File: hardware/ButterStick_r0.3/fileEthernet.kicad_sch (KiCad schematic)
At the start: 56 parts, among them CON1 JD1_0001NL, CON2 JD1_0001NL, Q7 PMBT3904MB, Q8 PMBT3904MB, U11 KSZ9031, Y1 25Mhz

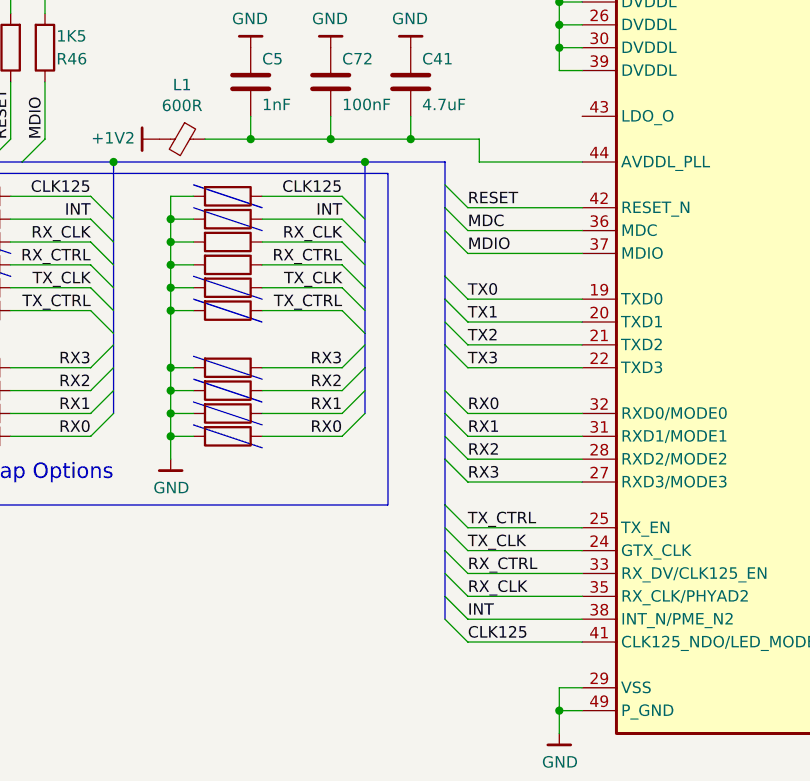
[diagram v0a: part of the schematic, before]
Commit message: hw.r0_3: routing improvements
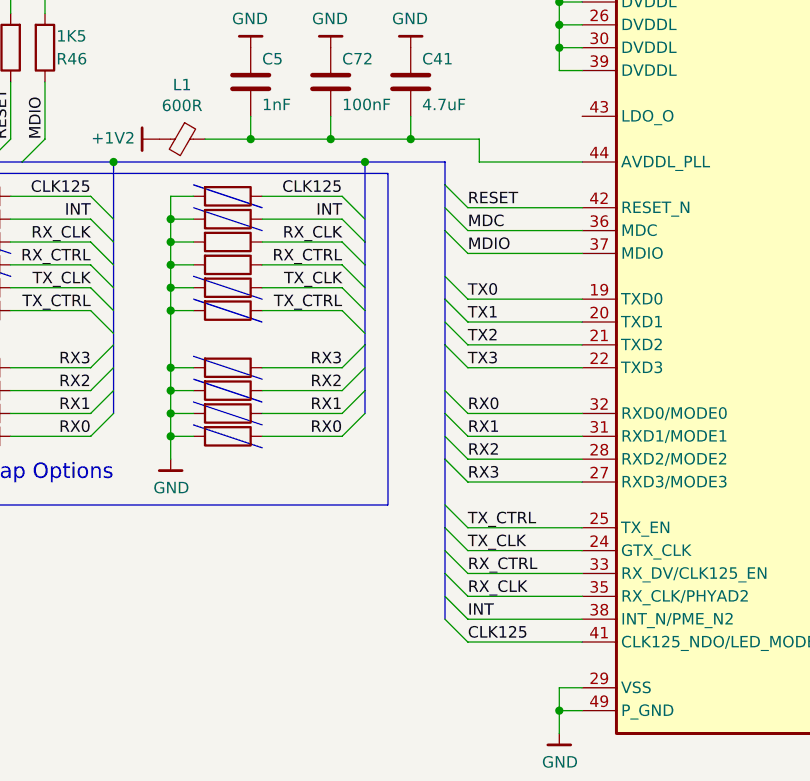
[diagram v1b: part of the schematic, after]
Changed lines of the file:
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@@
   (bus (pts (xy 111.76 91.44) (xy 111.76 100.33)))
   (bus (pts (xy 111.76 91.44) (xy 120.65 91.44)))
-  (bus (pts (xy 111.76 100.33) (xy 111.76 105.41)))
-  (bus (pts (xy 111.76 105.41) (xy 111.76 110.49)))
-  (bus (pts (xy 111.76 110.49) (xy 111.76 114.3)))
-  (bus (pts (xy 111.76 114.3) (xy 111.76 119.38)))
-  (bus (pts (xy 120.65 91.44) (xy 120.65 96.52)))
-  (bus (pts (xy 120.65 96.52) (xy 120.65 104.14)))
-  (bus (pts (xy 120.65 104.14) (xy 120.65 106.68)))
+  (bus (pts (xy 111.76 100.33) (xy 111.76 102.87)))
+  (bus (pts (xy 111.76 102.87) (xy 111.76 107.95)))
+  (bus (pts (xy 111.76 107.95) (xy 111.76 111.76)))
+  (bus (pts (xy 111.76 111.76) (xy 111.76 116.84)))
+  (bus (pts (xy 111.76 116.84) (xy 111.76 119.38)))
+  (bus (pts (xy 120.65 91.44) (xy 120.65 93.98)))
+  (bus (pts (xy 120.65 93.98) (xy 120.65 99.06)))
+  (bus (pts (xy 120.65 99.06) (xy 120.65 106.68)))
   (bus (pts (xy 120.65 106.68) (xy 120.65 111.76)))
   (bus (pts (xy 120.65 111.76) (xy 120.65 119.38)))
   (bus (pts (xy 120.65 119.38) (xy 120.65 124.46)))
-  (bus (pts (xy 120.65 124.46) (xy 120.65 129.54)))
-  (bus (pts (xy 120.65 129.54) (xy 120.65 134.62)))
-  (bus (pts (xy 120.65 134.62) (xy 120.65 139.7)))
-  (bus (pts (xy 120.65 139.7) (xy 120.65 142.24)))
+  (bus (pts (xy 120.65 124.46) (xy 120.65 132.08)))
+  (bus (pts (xy 120.65 132.08) (xy 120.65 137.16)))
+  (bus (pts (xy 120.65 137.16) (xy 120.65 142.24)))
   (polyline (pts (xy 59.69 92.71) (xy 59.69 129.54)))
   (polyline (pts (xy 59.69 92.71) (xy 114.3 92.71)))

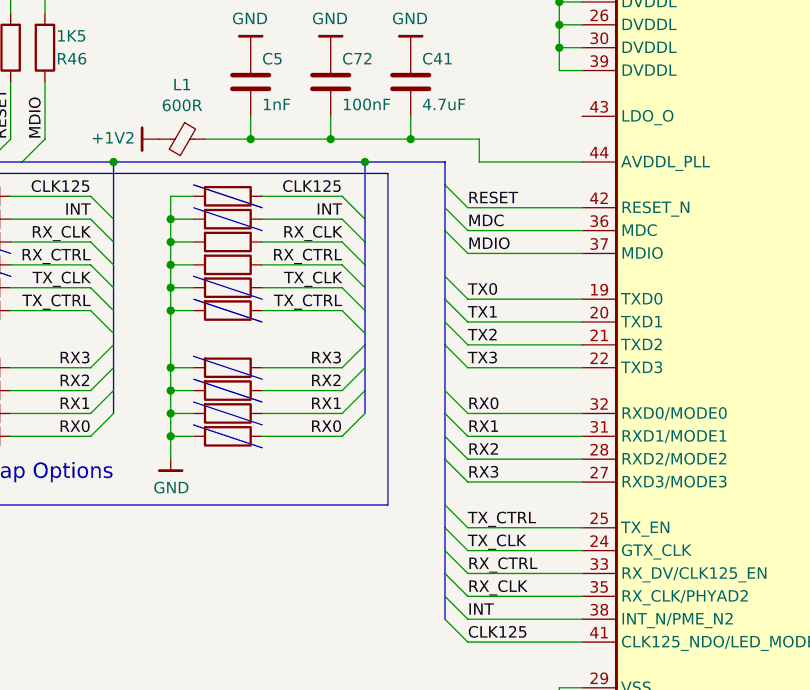
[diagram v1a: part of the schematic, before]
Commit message: hw.r0_3: Start routing DDR3 interface
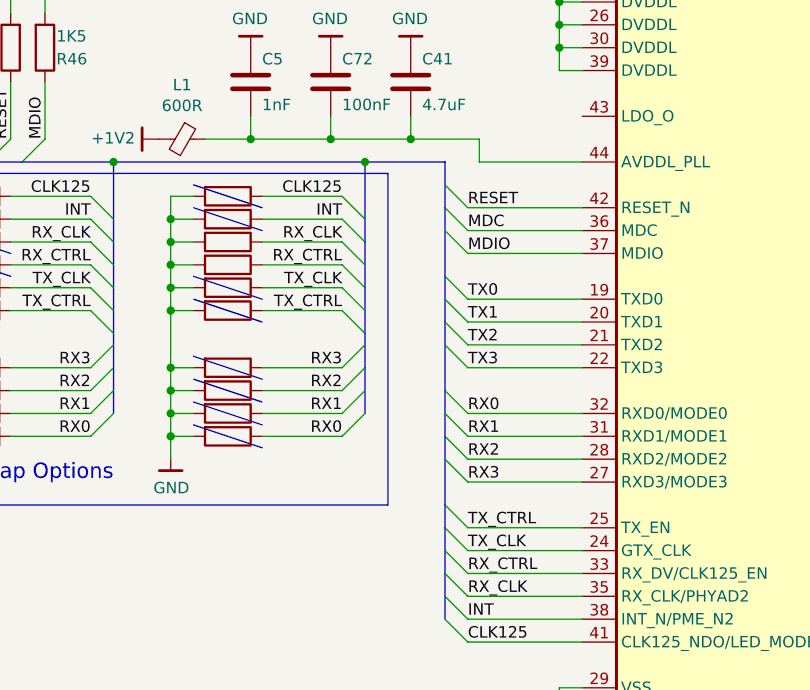
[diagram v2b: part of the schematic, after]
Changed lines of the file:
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@@
-(kicad_sch (version 20200512) (host eeschema "5.99.0-unknown-c8476d6~101~ubuntu18.04.1")
-  (page 3 20)
+(kicad_sch (version 20200512) (host eeschema "5.99.0-unknown-711fc99~101~ubuntu18.04.1")
+  (page 1 20)
   (paper "A4")
   (title_block
@@
   (bus (pts (xy 111.76 91.44) (xy 111.76 100.33)))
   (bus (pts (xy 111.76 91.44) (xy 120.65 91.44)))
-  (bus (pts (xy 111.76 100.33) (xy 111.76 102.87)))
-  (bus (pts (xy 111.76 102.87) (xy 111.76 107.95)))
-  (bus (pts (xy 111.76 107.95) (xy 111.76 111.76)))
-  (bus (pts (xy 111.76 111.76) (xy 111.76 116.84)))
-  (bus (pts (xy 111.76 116.84) (xy 111.76 119.38)))
-  (bus (pts (xy 120.65 91.44) (xy 120.65 93.98)))
-  (bus (pts (xy 120.65 93.98) (xy 120.65 99.06)))
-  (bus (pts (xy 120.65 99.06) (xy 120.65 106.68)))
-  (bus (pts (xy 120.65 106.68) (xy 120.65 111.76)))
-  (bus (pts (xy 120.65 111.76) (xy 120.65 119.38)))
-  (bus (pts (xy 120.65 119.38) (xy 120.65 124.46)))
-  (bus (pts (xy 120.65 124.46) (xy 120.65 132.08)))
+  (bus (pts (xy 111.76 100.33) (xy 111.76 105.41)))
+  (bus (pts (xy 111.76 105.41) (xy 111.76 110.49)))
+  (bus (pts (xy 111.76 110.49) (xy 111.76 114.3)))
+  (bus (pts (xy 111.76 114.3) (xy 111.76 119.38)))
+  (bus (pts (xy 120.65 91.44) (xy 120.65 96.52)))
+  (bus (pts (xy 120.65 96.52) (xy 120.65 104.14)))
+  (bus (pts (xy 120.65 104.14) (xy 120.65 109.22)))
+  (bus (pts (xy 120.65 109.22) (xy 120.65 116.84)))
+  (bus (pts (xy 120.65 116.84) (xy 120.65 121.92)))
+  (bus (pts (xy 120.65 121.92) (xy 120.65 129.54)))
+  (bus (pts (xy 120.65 129.54) (xy 120.65 132.08)))
   (bus (pts (xy 120.65 132.08) (xy 120.65 137.16)))
   (bus (pts (xy 120.65 137.16) (xy 120.65 142.24)))

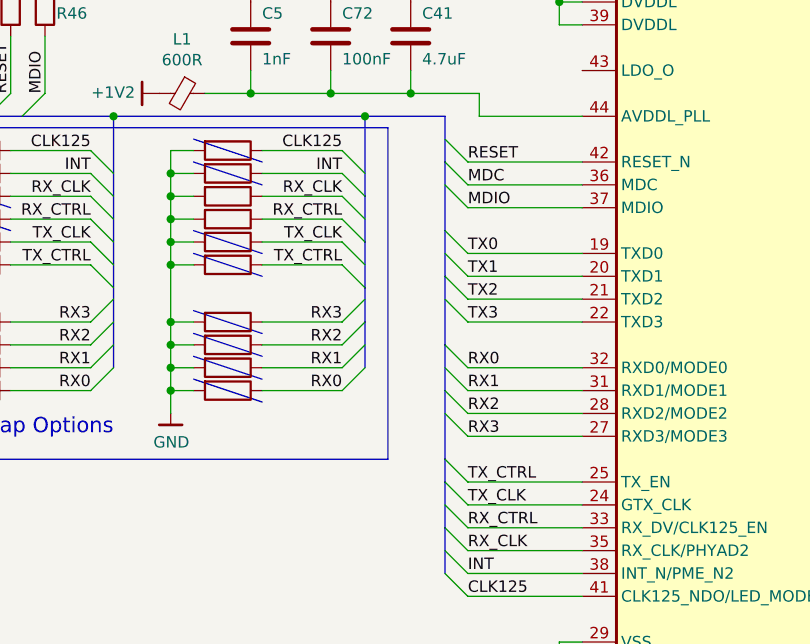
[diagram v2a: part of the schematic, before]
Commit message: hw.r0_3: Inital routing of DDR3 done
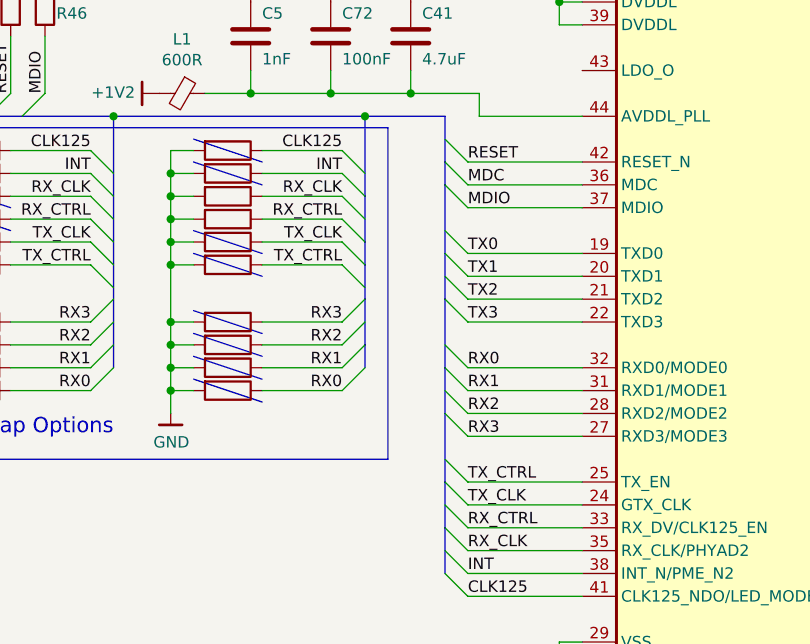
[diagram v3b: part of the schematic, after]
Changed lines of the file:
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@@
   (bus (pts (xy 111.76 91.44) (xy 120.65 91.44)))
   (bus (pts (xy 111.76 100.33) (xy 111.76 105.41)))
-  (bus (pts (xy 111.76 105.41) (xy 111.76 110.49)))
-  (bus (pts (xy 111.76 110.49) (xy 111.76 114.3)))
-  (bus (pts (xy 111.76 114.3) (xy 111.76 119.38)))
+  (bus (pts (xy 111.76 105.41) (xy 111.76 107.95)))
+  (bus (pts (xy 111.76 107.95) (xy 111.76 111.76)))
+  (bus (pts (xy 111.76 111.76) (xy 111.76 116.84)))
+  (bus (pts (xy 111.76 116.84) (xy 111.76 119.38)))
   (bus (pts (xy 120.65 91.44) (xy 120.65 96.52)))
-  (bus (pts (xy 120.65 96.52) (xy 120.65 104.14)))
-  (bus (pts (xy 120.65 104.14) (xy 120.65 109.22)))
-  (bus (pts (xy 120.65 109.22) (xy 120.65 116.84)))
-  (bus (pts (xy 120.65 116.84) (xy 120.65 121.92)))
-  (bus (pts (xy 120.65 121.92) (xy 120.65 129.54)))
-  (bus (pts (xy 120.65 129.54) (xy 120.65 132.08)))
+  (bus (pts (xy 120.65 96.52) (xy 120.65 99.06)))
+  (bus (pts (xy 120.65 99.06) (xy 120.65 106.68)))
+  (bus (pts (xy 120.65 106.68) (xy 120.65 111.76)))
+  (bus (pts (xy 120.65 111.76) (xy 120.65 119.38)))
+  (bus (pts (xy 120.65 119.38) (xy 120.65 124.46)))
+  (bus (pts (xy 120.65 124.46) (xy 120.65 132.08)))
   (bus (pts (xy 120.65 132.08) (xy 120.65 137.16)))
   (bus (pts (xy 120.65 137.16) (xy 120.65 142.24)))

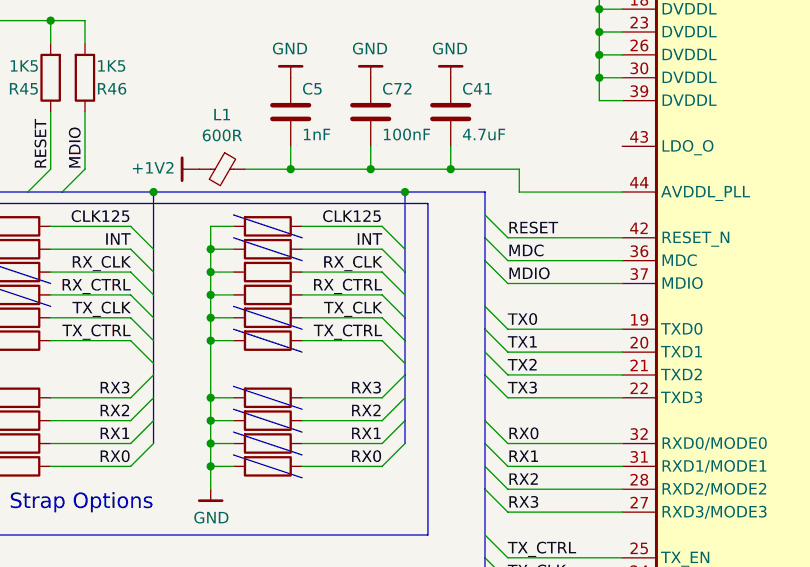
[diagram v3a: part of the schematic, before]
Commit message: hw.r0_3: routed SYZYGY, begin routing RGMII/ULPI
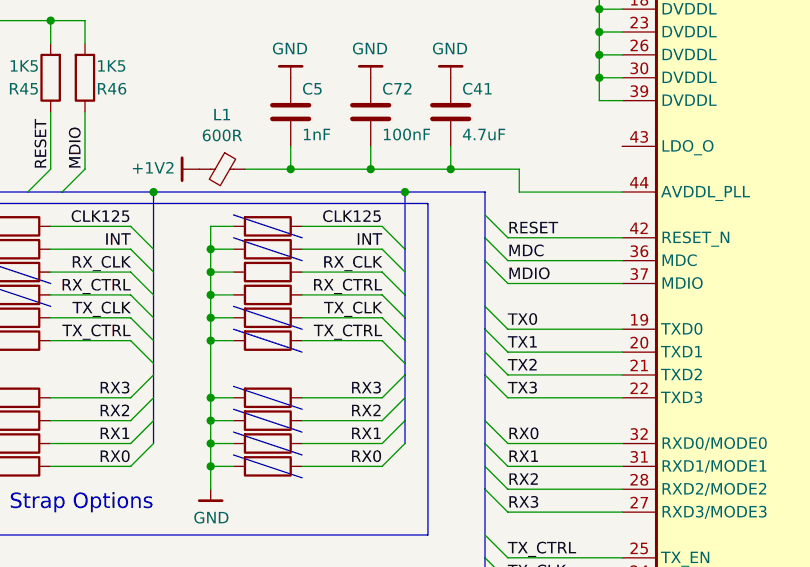
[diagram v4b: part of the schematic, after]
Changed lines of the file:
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@@
 (kicad_sch (version 20200512) (host eeschema "5.99.0-unknown-711fc99~101~ubuntu18.04.1")
-  (page 1 20)
+  (page 3 19)
   (paper "A4")
   (title_block
@@
   (bus (pts (xy 83.82 111.76) (xy 83.82 116.84)))
   (bus (pts (xy 83.82 116.84) (xy 83.82 119.38)))
-  (bus (pts (xy 111.76 91.44) (xy 111.76 100.33)))
+  (bus (pts (xy 111.76 91.44) (xy 111.76 97.79)))
   (bus (pts (xy 111.76 91.44) (xy 120.65 91.44)))
-  (bus (pts (xy 111.76 100.33) (xy 111.76 105.41)))
-  (bus (pts (xy 111.76 105.41) (xy 111.76 107.95)))
-  (bus (pts (xy 111.76 107.95) (xy 111.76 111.76)))
+  (bus (pts (xy 111.76 97.79) (xy 111.76 102.87)))
+  (bus (pts (xy 111.76 102.87) (xy 111.76 105.41)))
+  (bus (pts (xy 111.76 105.41) (xy 111.76 110.49)))
+  (bus (pts (xy 111.76 110.49) (xy 111.76 111.76)))
   (bus (pts (xy 111.76 111.76) (xy 111.76 116.84)))
   (bus (pts (xy 111.76 116.84) (xy 111.76 119.38)))

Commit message: hw.r0_3: major blocks roughly routed
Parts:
- removed C40: 4.7uF, Capacitor_SMD:C_0603_1608Metric, symbol Device:C
- removed C55: 10uF, Capacitor_SMD:C_0603_1608Metric, symbol Device:C
- removed CON1: JD1_0001NL, gkl_conn:MAGJACK, symbol gkl_misc:JD1_0001NL
- removed L3: 600R, pkl_dipol:L_0603, symbol Device:Ferrite_Bead_Small
- removed Q7, Q8: PMBT3904MB, Package_TO_SOT_SMD:SOT-883, symbol gkl_misc:PMBT3904MB
- removed R15, R24: 1k5, Resistor_SMD:R_0402_1005Metric, symbol Device:R
- removed R20, R21: 220R, Resistor_SMD:R_0402_1005Metric, symbol Device:R
- Y1: footprint Oscillators:Oscillator_SMD_SeikoEpson_SG210-4pin_2.5x2.0mm -> Oscillator:Oscillator_SMD_SeikoEpson_SG210-4Pin_2.5x2.0mm
- renumbered C41 to C10, C34 to C11, C26 to C12, C27 to C13, C29 to C14, C31 to C15, C33 to C16, C35 to C17, C37 to C18, C36 to C19, C25 to C4, C28 to C5, C5 to C6, C30 to C7, C72 to C8, C32 to C9, CON2 to CON1, L5 to L2, R39 to R10, R40 to R11, R41 to R12, R42 to R13, R43 to R14, R44 to R15, R45 to R16, R46 to R17, R48 to R18, R49 to R19, R50 to R20, R51 to R21, R52 to R22, R53 to R23, R54 to R24, R55 to R25, R56 to R26, R57 to R27, R19 to R28, R84 to R29, R85 to R30, R34 to R6, R36 to R7, R37 to R8, R38 to R9, U11 to U2
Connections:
- net +1V8 is gone; now on net +3V3: C11.1, C7.1, C9.1, R10.2, R11.2, R12.2, R13.2, R14.2, R15.2, R16.2, R17.2, R6.2, R7.2, R8.2, R9.2, U2.16 (DVDDH), U2.34 (DVDDH), U2.40 (DVDDH)
- net ETH_A_N: now also CON1.9 (P8), U2.3 (TXRXM_A)
- net ETH_A_P: now also CON1.10 (P9), U2.2 (TXRXP_A)
- net ETH_B_N: now also CON1.7 (P6), U2.6 (TXRXM_B)
- net ETH_B_P: now also CON1.8 (P7), U2.5 (TXRXP_B)
- net ETH_C_N: now also CON1.5 (P4), U2.8 (TXRXM_C)
- net ETH_C_P: now also CON1.6 (P5), U2.7 (TXRXP_C)
- net ETH_D_N: now also CON1.3 (P2), U2.11 (TXRXM_D)
- net ETH_D_P: now also CON1.4 (P3), U2.10 (TXRXP_D)
- net at U2.17 (LED1/PHYAD0/PME_N1): now also CON1.15 (YELLOW_K)
- net at U2.15 (LED2/PHYAD1): now also CON1.13 (GREEN_K)

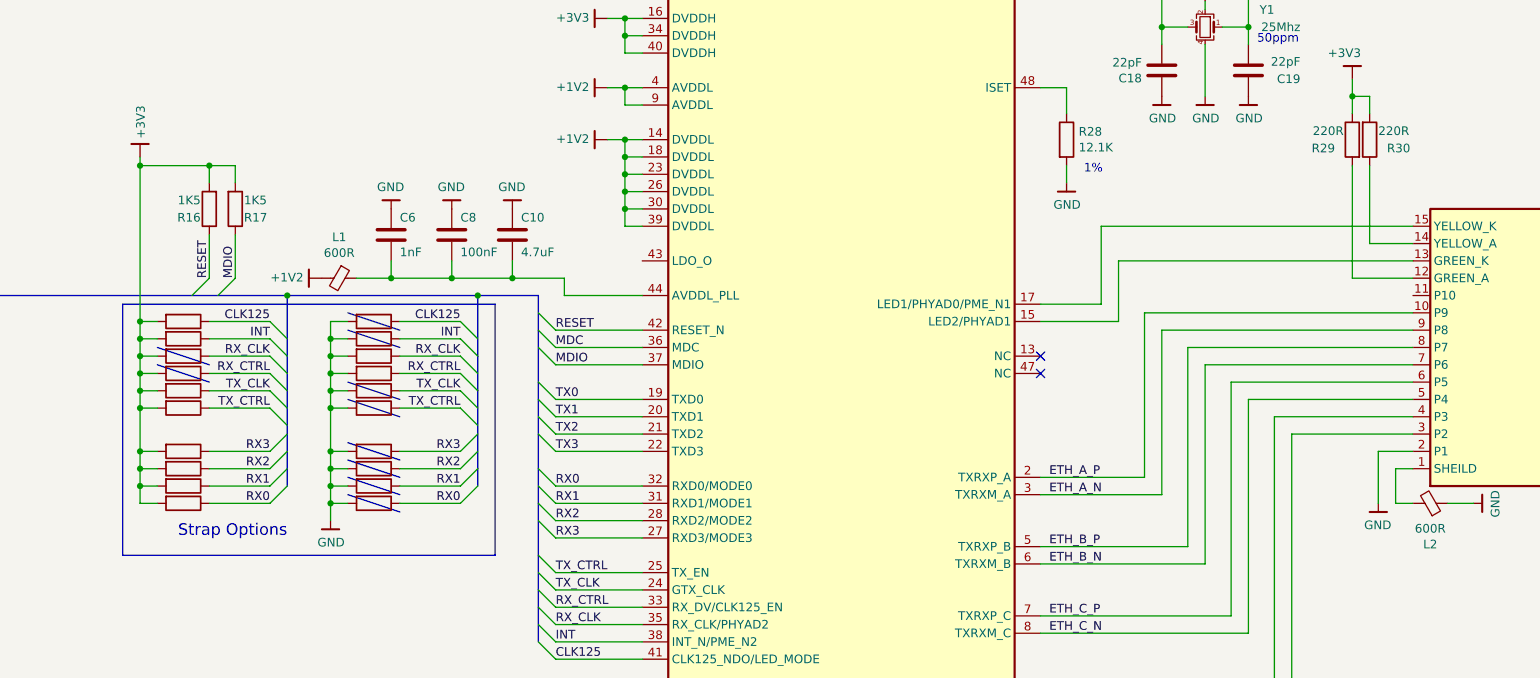
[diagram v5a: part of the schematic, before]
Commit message: hw.r0d3: Length matched all SYZYGY ports
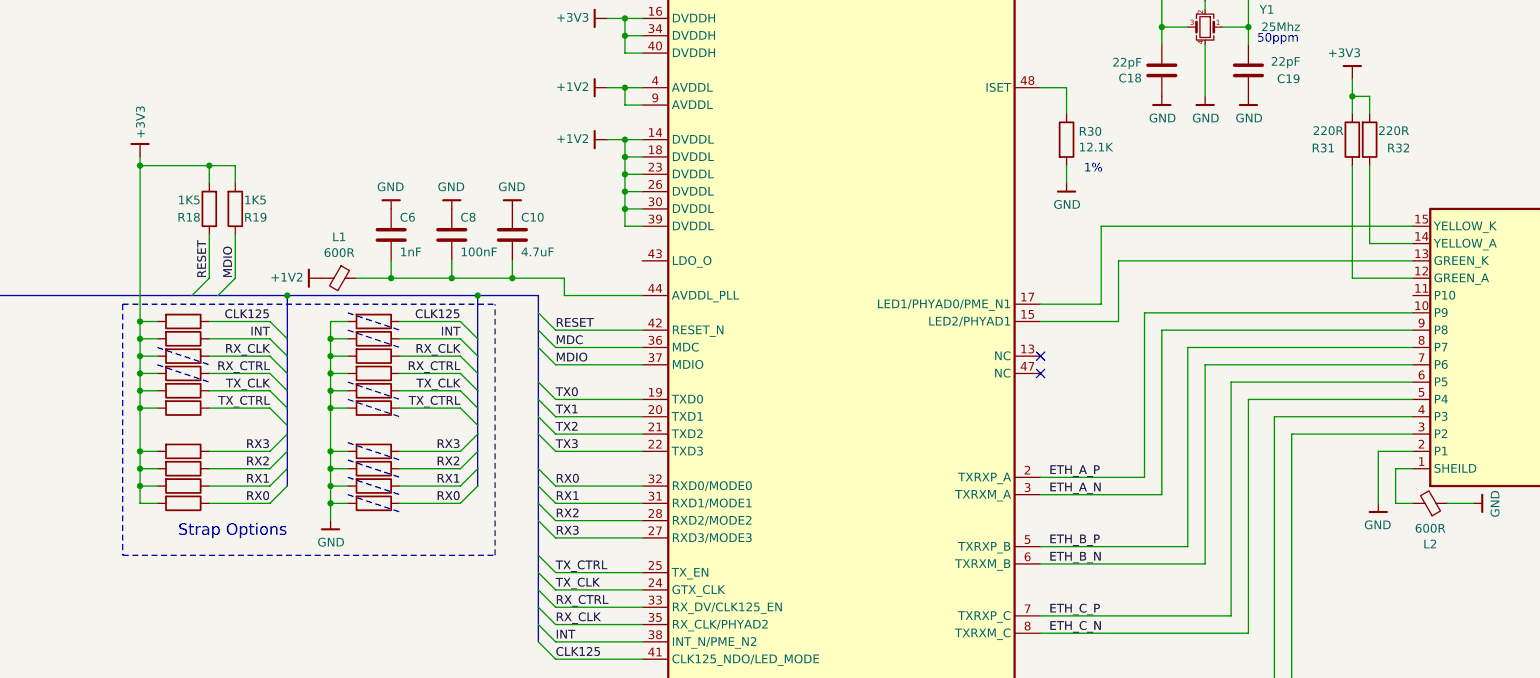
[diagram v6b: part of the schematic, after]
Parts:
- renumbered R8 to R10, R9 to R11, R10 to R12, R11 to R13, R12 to R14, R13 to R15, R14 to R16, R15 to R17, R16 to R18, R17 to R19, R18 to R20, R19 to R21, R20 to R22, R21 to R23, R22 to R24, R23 to R25, R24 to R26, R25 to R27, R26 to R28, R27 to R29, R28 to R30, R29 to R31, R30 to R32, R6 to R8, R7 to R9
